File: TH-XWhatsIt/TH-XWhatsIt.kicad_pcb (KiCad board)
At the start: 2 copper layers, 145.3 x 129.6 mm, 32 parts, among them J1 MODEL F, J2 EXPANSION, J3 EXPANSION HEADER, J4 EXPANSION BEAMSPRING, J5 BEAMSPRING CONNECTOR, J6 EXPANSION BEAMSPRING, J7 EXPANSION DISPLAYWRITER, J8 DISPLAYWRITER CONNECTOR, J9 EXPANSION DISPLAYWRITER, U1 MCP4921-EP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

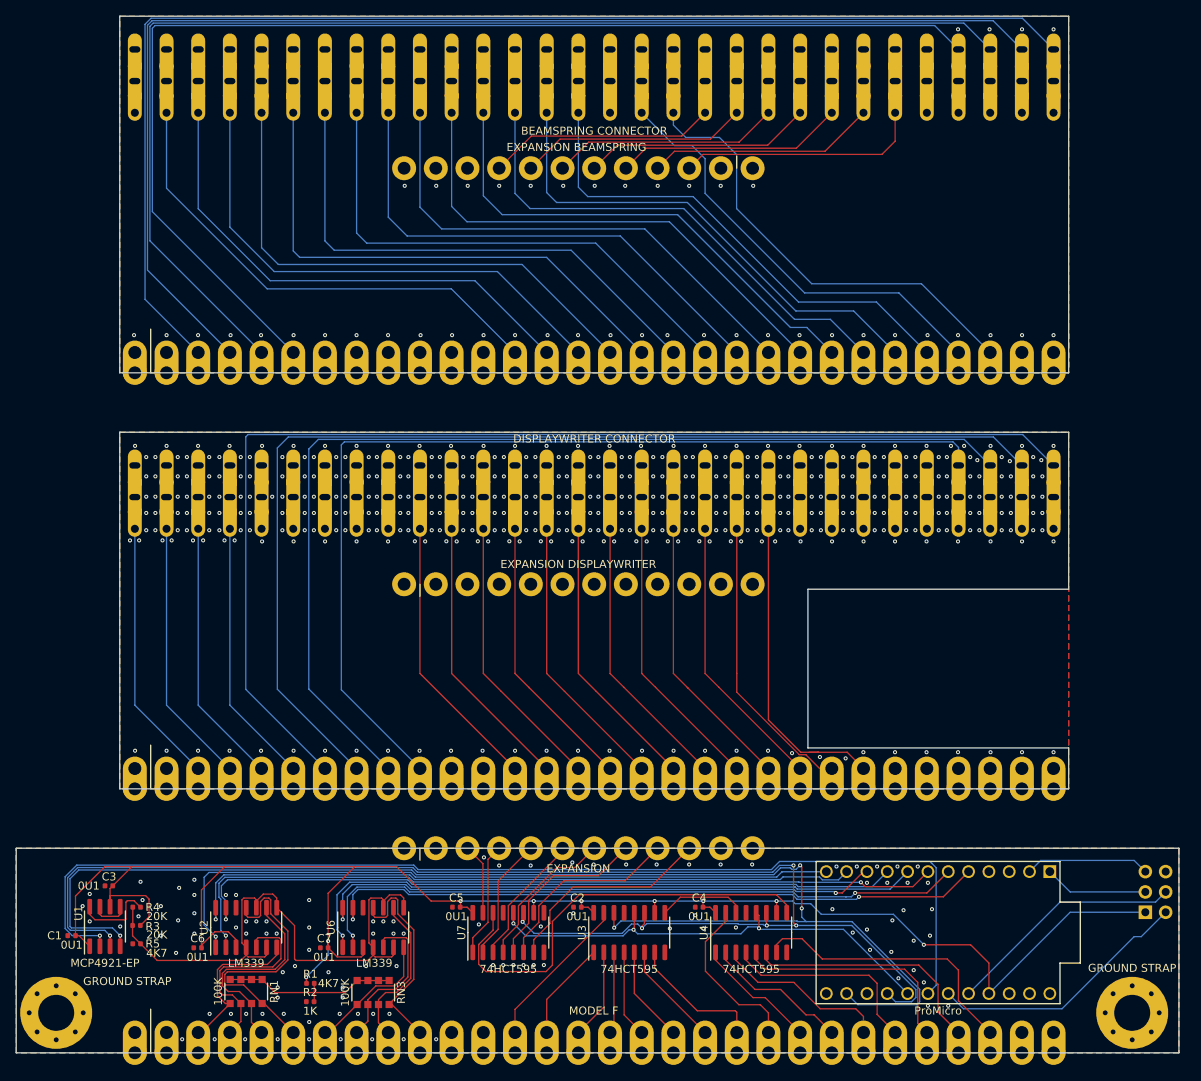
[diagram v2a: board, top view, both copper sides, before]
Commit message: Added cutout to the beamspring plugboard
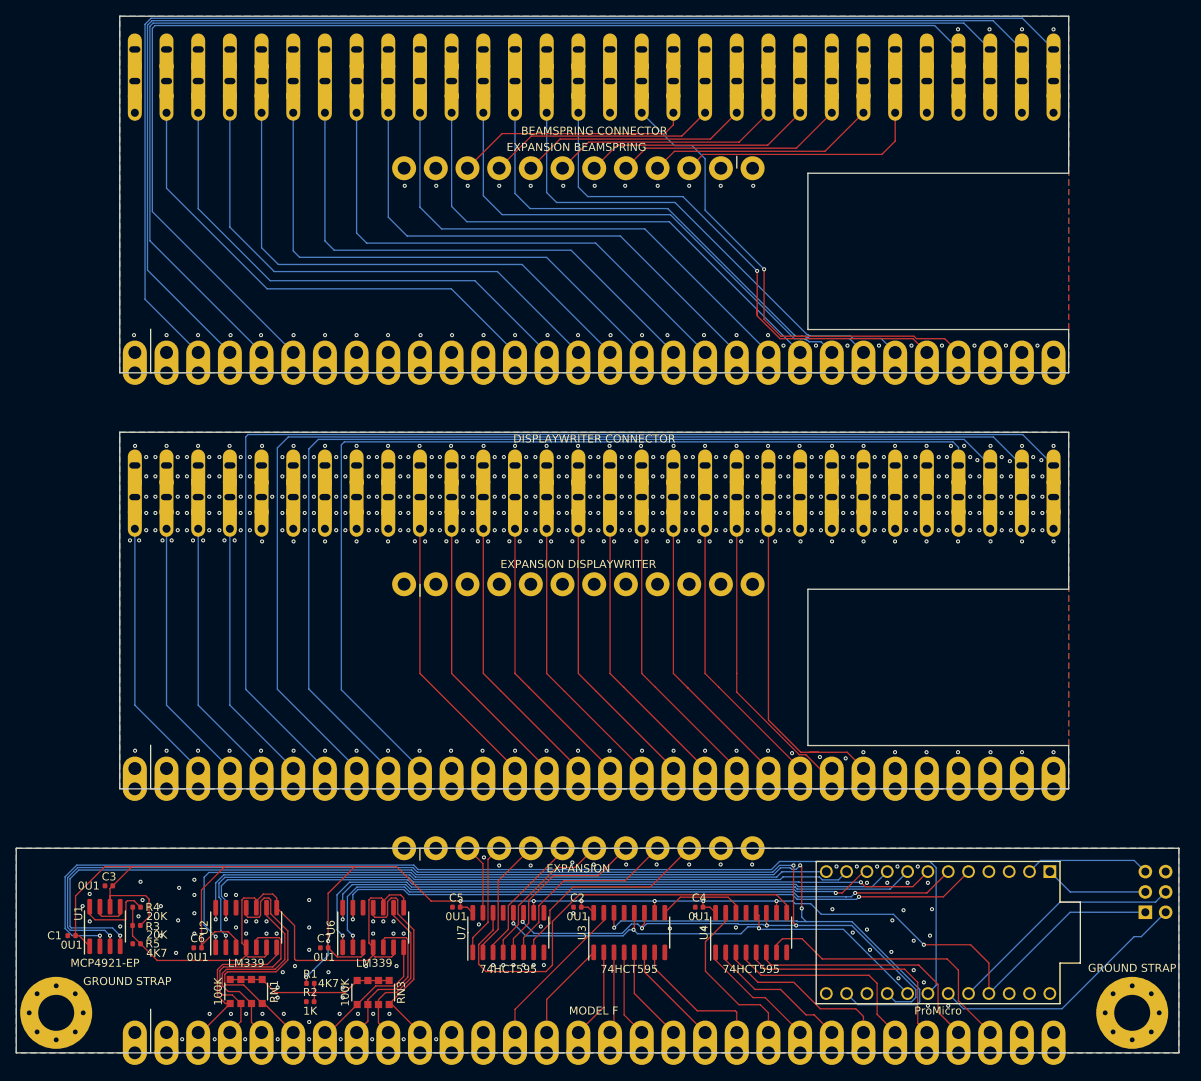
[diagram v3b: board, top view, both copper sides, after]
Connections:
- J4 pad 28: /beamspring plugboard/BSCOL16 -> Net-(J4-Pad28)
- J6 pad 10: Net-(J6-Pad10) -> /beamspring plugboard/BSCOL16
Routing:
- net /beamspring plugboard/BSCOL16: track 64.8 -> 37.4 mm
- net /beamspring plugboard/BSCOL15: track 62.5 -> 67.4 mm, vias 0 -> 1
- net /beamspring plugboard/BSCOL14: track 69.3 -> 73.3 mm, vias 0 -> 1
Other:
- outline, holes or cut-outs redrawn

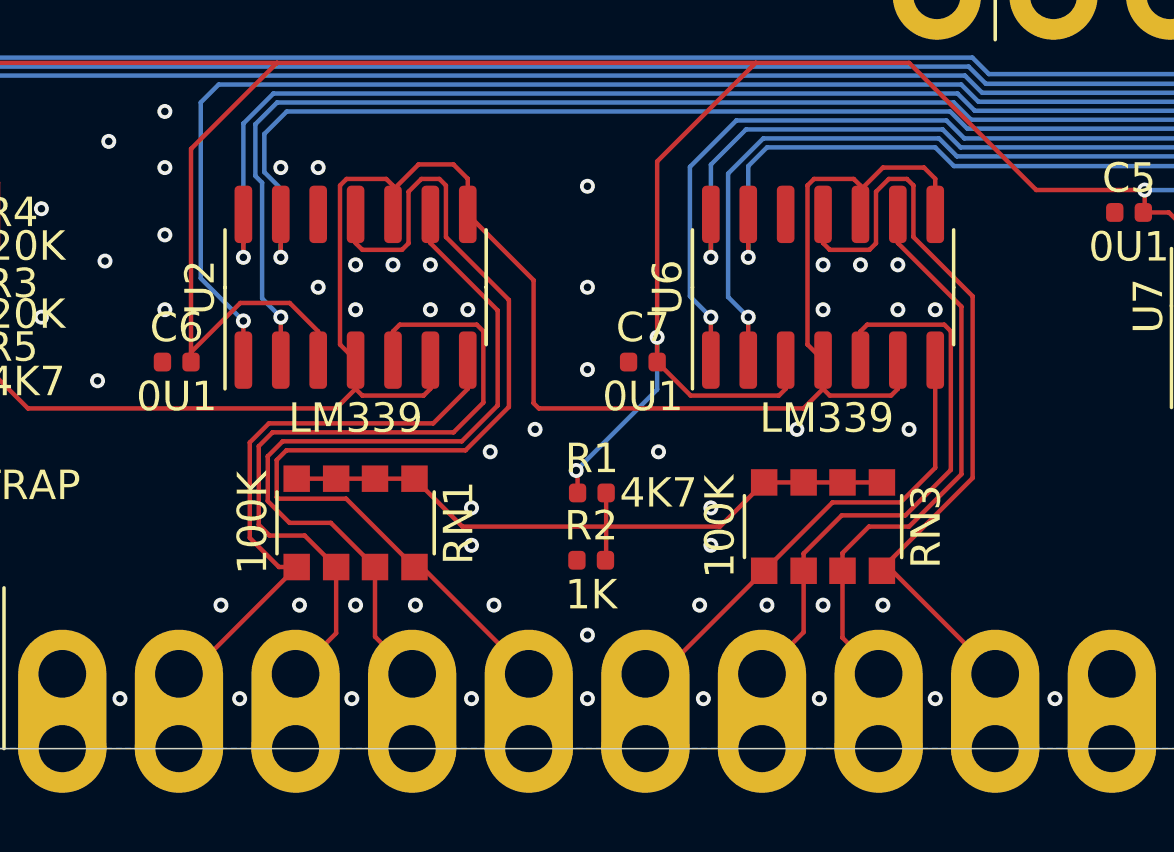
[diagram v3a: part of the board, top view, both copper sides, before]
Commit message: changed resistor network footprint sizes to what's available from jlcpcb
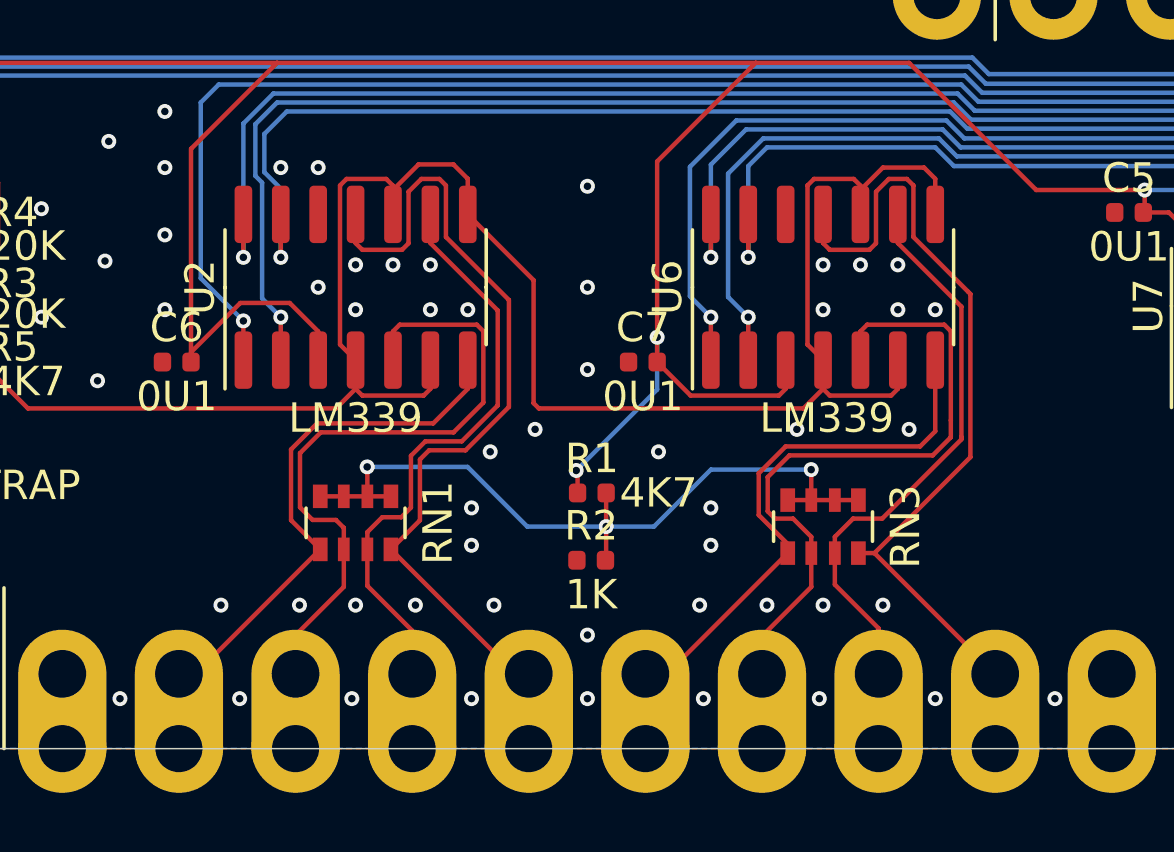
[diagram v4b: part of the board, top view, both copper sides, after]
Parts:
- RN1, RN3: footprint Resistor_SMD:R_Array_Convex_4x1206 -> Resistor_SMD:R_Array_Convex_4x0603
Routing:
- net SENSE4: track 35.6 -> 28.3 mm
- net SENSE3: track 26.2 -> 20.1 mm
- net SENSE7: track 19.8 -> 23.0 mm
- net SENSE5: track 16.4 -> 19.2 mm
- net BIAS: track 23.5 -> 25.9 mm, vias 0 -> 3
- net SENSE2: track 25.0 -> 22.8 mm
- net SENSE1: track 19.9 -> 18.6 mm
